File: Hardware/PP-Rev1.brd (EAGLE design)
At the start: 160 x 100 mm, 169 parts, among them IC1 LT6004, IC2 TLC6C5912-Q1, Q1 MOSFET-PCHANNEL, Q10 2N7002PW, Q11 2N7002PW, Q12 2N7002PW, Q13 2N7002PW, Q14 2N7002PW, Q15 2N7002PW, Q2 MOSFET-PCHANNEL, Q3 MOSFET-PCHANNEL, Q4 MOSFET-PCHANNEL, Q5 MOSFET-PCHANNEL, Q6 MOSFET-PCHANNEL, Q7 MOSFET-PCHANNEL, Q8 MOSFET-PCHANNEL, Q9 CSD18532, X1 22-23-2031, X2 22-23-2031, X3 22-23-2031, X4 22-23-2031

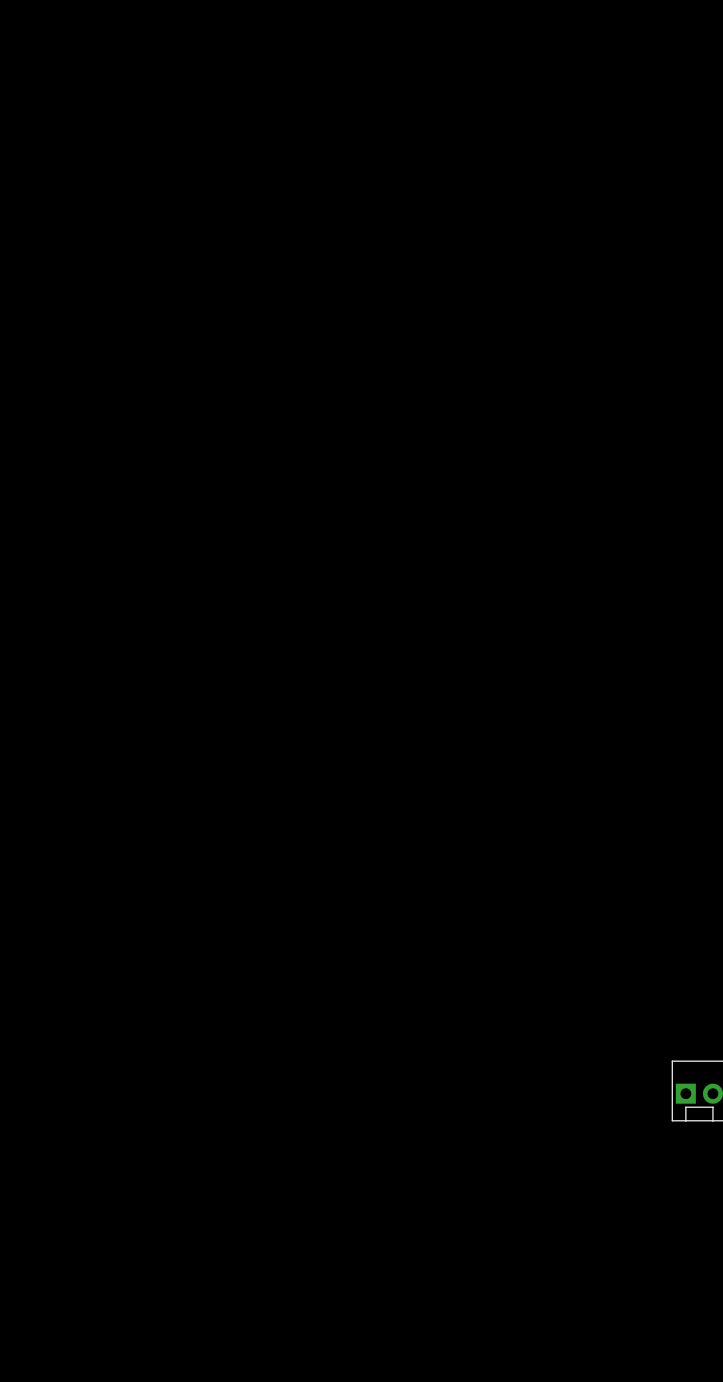
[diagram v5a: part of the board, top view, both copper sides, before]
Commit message: Added launchpad microcontroller library file and into schematic/board. Updated LCD connections to better utilize microcontroller port architecture
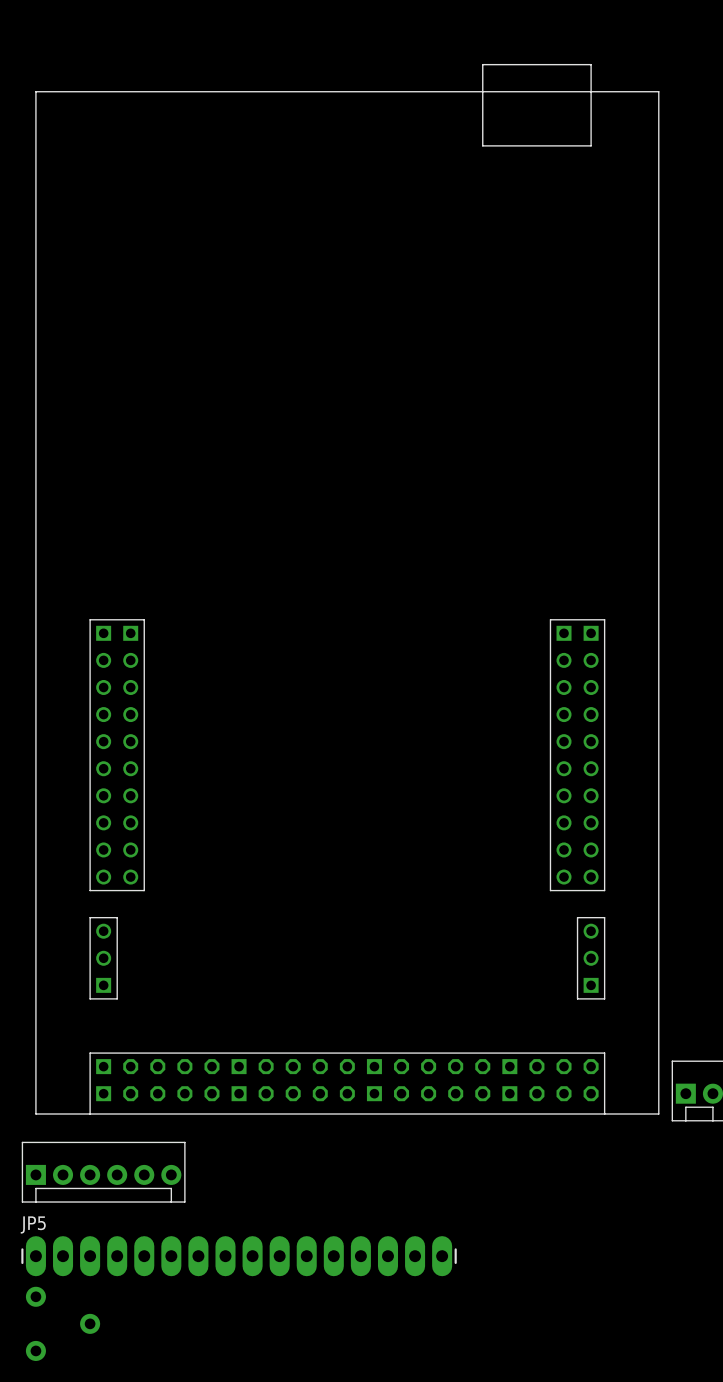
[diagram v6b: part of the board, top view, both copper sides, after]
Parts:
- added JP4: JST B6B-XH, SparkFun-Connectors:MOLEX-1X6
- added JP5: (no value), SparkFun-Connectors:1X16_LONGPADS
- added RV1: (no value), SparkFun-Electromechanical:TRIM_POT
- added U$13: MSP432P401R-LAUNCHPAD, 2016PowerPackLibraries:MSP432P401R-LAUNCHPAD
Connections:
- removed net N$62: GAUGE_ON.2, IC2.P$10, R57.2, S2.3
- removed net V_OUT: R38.2, R39.1
- new net CHARGER+: CHARGER+.P$1, JP4.4, Q9.2, Q9.4, R43.2, U$10.+, U$11.+
- new net GAUGE_ON: GAUGE_ON.2, IC2.P$10, R57.2, S2.3, U$13.6.6
- new net LCD_DB[0]: JP5.7, U$13.4.0
- new net LCD_DB[1]: JP5.8, U$13.4.1
- new net LCD_DB[2]: JP5.9, U$13.4.2
- new net LCD_DB[3]: JP5.10, U$13.4.3
- new net LCD_DB[4]: JP5.11, U$13.4.4
- new net LCD_DB[5]: JP5.12, U$13.4.5
- new net LCD_DB[6]: JP5.13, U$13.4.6
- new net LCD_DB[7]: JP5.14, U$13.4.7
- new net LCD_EN: JP5.6, U$13.3.7
- new net LCD_RS: JP5.4, U$13.3.5
- new net LCD_RW: JP5.5, U$13.3.6
- new net LCD_VBACK: JP5.3, RV1.1
- new net N$106: U$13.6.1
- new net N$107: U$13.6.2
- new net N$108: U$13.6.3
- new net N$109: U$13.6.4
- new net N$110: U$13.6.5
- new net N$115: JP5.15
- new net N$116: JP5.16
- new net N$45: U$13.9.4
- new net N$67: U$13.9.5
- new net N$68: U$13.9.6
- new net N$93: U$13.9.7
- new net SUPPLY_CTL: JP4.6, U$13.2.3
- new net SUPPLY_DC_OK: JP4.1, U$13.1.7
- new net V_CHECK_OUT: R38.2, R39.1, U$13.5.4
- net 5V: now also JP5.2, RV1.3, U$13.5V_1, U$13.5V_2, U$13.5V_3, U$13.5V_4
- net BUZZ_1: now also U$13.5.6
- net BUZZ_2: now also U$13.5.7
- net CHARGER_CTL: now also U$13.8.0
- net CHARGER_I_MEAS: now also U$13.5.2
- net ESTOP_1: now also U$13.1.5
- net ESTOP_2: now also U$13.1.6
- net FAN_CTL_1: now also U$13.2.4
- net FAN_CTL_2: now also U$13.2.5
- net FAN_CTL_3: now also U$13.2.6
- net FAN_CTL_4: now also U$13.2.7
- net FAN_TACH_1: now also U$13.5.0
- net FAN_TACH_2: now also U$13.3.3
- net FAN_TACH_3: now also U$13.3.2
- net FAN_TACH_4: now also U$13.3.0
- net GND: now also JP4.2, JP4.3, JP4.5, JP5.1, RV1.2, U$13.GND_1, U$13.GND_2, U$13.GND_3, U$13.GND_4, U$13.GND_5, U$13.GND_6, U$13.GND_7, U$13.GND_8
- net LED_CLR: now also U$13.10.0
- net LED_RCK: now also U$13.10.1
- net LED_SER_IN: now also U$13.10.2
- net LED_SRCK: now also U$13.10.3
- net N$35: now also U$13.9.0; no longer CHARGER+.P$1, Q9.2, Q9.4, R43.2, U$10.+, U$11.+
- net PACK_GATE: now also U$13.6.0
- net PACK_I_MEAS: now also U$13.5.5
- net V_CHECK_ARRAY: now also U$13.5.3
- net V_CHECK_CHARGER_IN: now also U$13.5.1
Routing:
- added copper zone on layer 1, net CHARGER+
- removed copper zone on layer 1, net N$35

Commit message: Added Wiznet module
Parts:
- added U1: WIZ811MJ, SparkFun-Boards:WIZ811MJ
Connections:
- removed net N$106: U$13.6.1
- removed net N$35: U$13.9.0
- removed net N$45: U$13.9.4
- removed net N$67: U$13.9.5
- removed net N$68: U$13.9.6
- removed net N$93: U$13.9.7
- new net +3V3: U$13.3V3_1, U$13.3V3_2, U$13.3V3_3, U$13.3V3_4, U1.12, U1.21
- new net WIZNET_DATA_INT: U$13.6.1, U1.28
- new net WIZNET_MISO: U$13.9.6, U1.2
- new net WIZNET_MOSI: U$13.9.7, U1.1
- new net WIZNET_RESET: U$13.9.0, U1.22
- new net WIZNET_SCLK: U$13.9.5, U1.23
- new net WIZNET_SS: U$13.9.4, U1.24
- net GND: now also U1.11, U1.29, U1.30, U1.39, U1.40
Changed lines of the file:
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@@
 <element name="JP5" library="SparkFun-Connectors" package="1X16_LONGPADS" value="" x="-257.81" y="-92.71"/>
 <element name="RV1" library="SparkFun-Electromechanical" package="TRIM_POT" value="" x="-257.81" y="-99.06"/>
+<element name="U1" library="SparkFun-Boards" package="WIZ811MJ" value="WIZ811MJ" x="-227.33" y="-104.14"/>
 </elements>
 <signals>
@@
 <contactref element="JP5" pad="1"/>
 <contactref element="RV1" pad="2"/>
+<contactref element="U1" pad="30"/>
+<contactref element="U1" pad="40"/>
+<contactref element="U1" pad="39"/>
+<contactref element="U1" pad="29"/>
+<contactref element="U1" pad="11"/>
 <wire x1="-205.74" y1="-62.23" x2="-205.74" y2="-34.29" width="0" layer="19" extent="1-1"/>
 <wire x1="-205.74" y1="-64.77" x2="-205.74" y2="-62.23" width="0" layer="19" extent="1-1"/>
@@
 <wire x1="-257.81" y1="-92.71" x2="-255.27" y2="-85.09" width="0" layer="19" extent="1-1"/>
 <wire x1="-257.81" y1="-96.52" x2="-257.81" y2="-92.71" width="0" layer="19" extent="1-1"/>
+<wire x1="-240.03" y1="-104.14" x2="-257.81" y2="-96.52" width="0" layer="19" extent="1-1"/>
+<wire x1="-237.49" y1="-124.06" x2="-240.03" y2="-104.14" width="0" layer="19" extent="1-1"/>
+<wire x1="-237.49" y1="-126.6" x2="-237.49" y2="-124.06" width="0" layer="19" extent="1-1"/>
+<wire x1="-250.19" y1="-126.6" x2="-237.49" y2="-126.6" width="0" layer="19" extent="1-1"/>
+<wire x1="-250.19" y1="-124.06" x2="-250.19" y2="-126.6" width="0" layer="19" extent="1-1"/>
 <wire x1="-251.46" y1="-64.77" x2="-252.73" y2="-85.09" width="0" layer="19" extent="1-1"/>
 <wire x1="-251.46" y1="-62.23" x2="-251.46" y2="-64.77" width="0" layer="19" extent="1-1"/>
@@
 <wire x1="-208.28" y1="-49.53" x2="-245.11" y2="-85.09" width="0" layer="19" extent="1-1"/>
 </signal>
-<signal name="N$106">
+<signal name="WIZNET_DATA_INT">
 <contactref element="U$13" pad="6.1"/>
+<contactref element="U1" pad="28"/>
+<wire x1="-248.92" y1="-39.37" x2="-234.95" y2="-126.6" width="0" layer="19" extent="1-1"/>
 </signal>
 <signal name="N$107">
@@
 <contactref element="U$13" pad="6.5"/>
 </signal>
-<signal name="N$35">
+<signal name="WIZNET_RESET">
 <contactref element="U$13" pad="9.0"/>
-</signal>
-<signal name="N$45">
+<contactref element="U1" pad="22"/>
+<wire x1="-248.92" y1="-74.93" x2="-227.33" y2="-126.6" width="0" layer="19" extent="1-1"/>
+</signal>
+<signal name="WIZNET_SS">
 <contactref element="U$13" pad="9.4"/>
-</signal>
-<signal name="N$67">
+<contactref element="U1" pad="24"/>
+<wire x1="-231.14" y1="-74.93" x2="-229.87" y2="-126.6" width="0" layer="19" extent="1-1"/>
+</signal>
+<signal name="WIZNET_SCLK">
 <contactref element="U$13" pad="9.5"/>
-</signal>
-<signal name="N$68">
+<contactref element="U1" pad="23"/>
+<wire x1="-228.6" y1="-77.47" x2="-229.87" y2="-124.06" width="0" layer="19" extent="1-1"/>
+</signal>
+<signal name="WIZNET_MISO">
 <contactref element="U$13" pad="9.6"/>
-</signal>
-<signal name="N$93">
+<contactref element="U1" pad="2"/>
+<wire x1="-228.6" y1="-74.93" x2="-227.33" y2="-106.68" width="0" layer="19" extent="1-1"/>
+</signal>
+<signal name="WIZNET_MOSI">
 <contactref element="U$13" pad="9.7"/>
+<contactref element="U1" pad="1"/>
+<wire x1="-226.06" y1="-77.47" x2="-227.33" y2="-104.14" width="0" layer="19" extent="1-1"/>
 </signal>
 <signal name="LCD_VBACK">
@@
 <contactref element="JP5" pad="16"/>
 </signal>
+<signal name="+3V3">
+<contactref element="U$13" pad="3V3_4"/>
+<contactref element="U$13" pad="3V3_3"/>
+<contactref element="U$13" pad="3V3_2"/>
+<contactref element="U$13" pad="3V3_1"/>
+<contactref element="U1" pad="21"/>
+<contactref element="U1" pad="12"/>
+<wire x1="-240.03" y1="-106.68" x2="-227.33" y2="-124.06" width="0" layer="19" extent="1-1"/>
+<wire x1="-208.28" y1="-77.47" x2="-240.03" y2="-106.68" width="0" layer="19" extent="1-1"/>
+<wire x1="-208.28" y1="-74.93" x2="-208.28" y2="-77.47" width="0" layer="19" extent="1-1"/>
+<wire x1="-205.74" y1="-67.31" x2="-208.28" y2="-74.93" width="0" layer="19" extent="1-1"/>
+<wire x1="-251.46" y1="-34.29" x2="-205.74" y2="-67.31" width="0" layer="19" extent="1-1"/>
+</signal>
 </signals>

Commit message: Added communication between BMS front-end and microcontroller. Schematic functionally complete.
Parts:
- added R68: 1k, rcl:R1206
- added R69, R70, R71: 1M, rcl:R1206
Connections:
- removed net N$107: U$13.6.2
- removed net N$108: U$13.6.3
- removed net N$109: U$13.6.4
- removed net N$110: U$13.6.5
- new net BMS_CSBI: R69.2, U$1.44, U$13.6.2
- new net BMS_MISO: R68.1, U$1.43, U$13.6.5
- new net BMS_MOSI: R70.2, U$1.42, U$13.6.4
- new net BMS_SCLK: R71.2, U$1.41, U$13.6.3
- net +3V3: now also R68.2
- net BMS_VREG: now also R69.1, R70.1, R71.1
- net GND: now also U$1.35, U$1.36
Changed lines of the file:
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@@
 <element name="RV1" library="SparkFun-Electromechanical" package="TRIM_POT" value="" x="-257.81" y="-99.06"/>
 <element name="U1" library="SparkFun-Boards" package="WIZ811MJ" value="WIZ811MJ" x="-227.33" y="-104.14"/>
+<element name="R68" library="rcl" package="R1206" value="1k" x="-256.54" y="-132.08"/>
+<element name="R69" library="rcl" package="R1206" value="1M" x="-256.54" y="-138.43"/>
+<element name="R70" library="rcl" package="R1206" value="1M" x="-256.54" y="-144.78"/>
+<element name="R71" library="rcl" package="R1206" value="1M" x="-256.54" y="-151.13"/>
 </elements>
 <signals>
@@
 <contactref element="U1" pad="29"/>
 <contactref element="U1" pad="11"/>
+<contactref element="U$1" pad="35"/>
+<contactref element="U$1" pad="36"/>
 <wire x1="-205.74" y1="-62.23" x2="-205.74" y2="-34.29" width="0" layer="19" extent="1-1"/>
 <wire x1="-205.74" y1="-64.77" x2="-205.74" y2="-62.23" width="0" layer="19" extent="1-1"/>
@@
 <wire x1="169.67" y1="59.4" x2="169.67" y2="59.9" width="0" layer="19" extent="1-1"/>
 <wire x1="169.67" y1="58.9" x2="169.67" y2="59.4" width="0" layer="19" extent="1-1"/>
-<wire x1="169.67" y1="56.4" x2="169.67" y2="58.9" width="0" layer="19" extent="1-1"/>
+<wire x1="169.67" y1="58.4" x2="169.67" y2="58.9" width="0" layer="19" extent="1-1"/>
+<wire x1="169.67" y1="57.9" x2="169.67" y2="58.4" width="0" layer="19" extent="1-1"/>
+<wire x1="169.67" y1="56.4" x2="169.67" y2="57.9" width="0" layer="19" extent="1-1"/>
 <wire x1="169.67" y1="53.4" x2="169.67" y2="56.4" width="0" layer="19" extent="1-1"/>
 <wire x1="173.23" y1="27.94" x2="155.575" y2="30.6" width="0" layer="19" extent="1-1"/>
@@
 <contactref element="IC1" pad="8"/>
 <contactref element="C9" pad="1"/>
+<contactref element="R71" pad="1"/>
+<contactref element="R70" pad="1"/>
+<contactref element="R69" pad="1"/>
 <wire x1="169.67" y1="55.9" x2="168.482" y2="69.556" width="0" layer="19" extent="1-1"/>
 <wire x1="-124.59" y1="139.7" x2="168.482" y2="69.556" width="0" layer="19" extent="1-1"/>
+<wire x1="-257.962" y1="-138.43" x2="-124.59" y2="139.7" width="0" layer="19" extent="1-1"/>
+<wire x1="-257.962" y1="-144.78" x2="-257.962" y2="-138.43" width="0" layer="19" extent="1-1"/>
+<wire x1="-257.962" y1="-151.13" x2="-257.962" y2="-144.78" width="0" layer="19" extent="1-1"/>
 </signal>
 <signal name="BMS_VREF">
@@
 <wire x1="-248.92" y1="-39.37" x2="-234.95" y2="-126.6" width="0" layer="19" extent="1-1"/>
 </signal>
-<signal name="N$107">
+<signal name="BMS_CSBI">
 <contactref element="U$13" pad="6.2"/>
-</signal>
-<signal name="N$108">
+<contactref element="U$1" pad="44"/>
+<contactref element="R69" pad="2"/>
+<wire x1="-238.76" y1="-74.93" x2="169.67" y2="62.4" width="0" layer="19" extent="1-1"/>
+<wire x1="-255.118" y1="-138.43" x2="-238.76" y2="-74.93" width="0" layer="19" extent="1-1"/>
+</signal>
+<signal name="BMS_SCLK">
 <contactref element="U$13" pad="6.3"/>
-</signal>
-<signal name="N$109">
+<contactref element="U$1" pad="41"/>
+<contactref element="R71" pad="2"/>
+<wire x1="-236.22" y1="-77.47" x2="169.67" y2="60.9" width="0" layer="19" extent="1-1"/>
+<wire x1="-255.118" y1="-151.13" x2="-236.22" y2="-77.47" width="0" layer="19" extent="1-1"/>
+</signal>
+<signal name="BMS_MOSI">
 <contactref element="U$13" pad="6.4"/>
-</signal>
-<signal name="N$110">
+<contactref element="U$1" pad="42"/>
+<contactref element="R70" pad="2"/>
+<wire x1="-251.46" y1="-57.15" x2="169.67" y2="61.4" width="0" layer="19" extent="1-1"/>
+<wire x1="-255.118" y1="-144.78" x2="-251.46" y2="-57.15" width="0" layer="19" extent="1-1"/>
+</signal>
+<signal name="BMS_MISO">
 <contactref element="U$13" pad="6.5"/>
+<contactref element="U$1" pad="43"/>
+<contactref element="R68" pad="1"/>
+<wire x1="-251.46" y1="-54.61" x2="169.67" y2="61.9" width="0" layer="19" extent="1-1"/>
+<wire x1="-257.962" y1="-132.08" x2="-251.46" y2="-54.61" width="0" layer="19" extent="1-1"/>
 </signal>
 <signal name="WIZNET_RESET">
@@
 <contactref element="U1" pad="21"/>
 <contactref element="U1" pad="12"/>
+<contactref element="R68" pad="2"/>
+<wire x1="-227.33" y1="-124.06" x2="-255.118" y2="-132.08" width="0" layer="19" extent="1-1"/>
 <wire x1="-240.03" y1="-106.68" x2="-227.33" y2="-124.06" width="0" layer="19" extent="1-1"/>
 <wire x1="-208.28" y1="-77.47" x2="-240.03" y2="-106.68" width="0" layer="19" extent="1-1"/>
